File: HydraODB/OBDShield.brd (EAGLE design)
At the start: 59.9 x 37 mm, 10 parts, among them J1 HYDRABUS_SHIELD_CON_HEADER_2X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, J2 HYDRABUS_SHIELD_CON_HEADER_2X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, J3 HYDRABUS_SHIELD_CON_HEADER_2X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, U1 SN65HVD233DG4, U2 SN65HVD233DG4

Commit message: Mistake :-D
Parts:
- added JP1, JP2: (no value), jumper:JP1
- added LPWR, LRXCAN1, LRXCAN2, LTXCAN1, LTXCAN2: (no value), led:CHIPLED_0603
- added R3, R4, R5, R6, R7, R8, R9: (no value), resistor:R0603
- IC1: value (none) -> LM317MABDT; device v-reg:78XXS -> v-reg:DPACK
- moved U1 3.98 mm to (28.8, 14.6), flipped to the top, turned to 90 degrees
- moved SV1 2.41 mm to (4.70, 16.5)
- moved R1 2.32 mm to (18.8, 5.46)
- moved IC1 2.16 mm to (6.48, 30.7), turned to 90 degrees
- moved R2 1.30 mm to (18.0, 31.6)
- moved U2 1.17 mm to (28.8, 23.6), flipped to the top, turned to 90 degrees
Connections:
- new net N$13: LTXCAN1.A, R5.2
- new net N$14: LPWR.A, R3.1
- new net N$15: R3.2
- new net N$16: JP2.1, R9.2
- new net N$19: JP1.1, R8.2
- new net N$7: LRXCAN1.A, R4.2
- new net PB11: J1.4, R9.1, U2.1
- new net PB6: J1.12
- new net PB9: J1.2, JP2.2, U2.4
- net +12V: now also IC1.3, SV1.7, SV1.8; no longer IC1.IN
- net GND: now also IC1.1, LPWR.C, LTXCAN1.C; no longer IC1.GND
- net PB10: now also J1.6, JP1.2, R5.1; no longer J1.8
- net PB5: no longer U2.4
- net PB7: now also J1.10; no longer J1.12, U2.1
- net PB8: now also J1.8, R4.1, R8.1; no longer J1.6
- net VUSB: now also IC1.4; no longer IC1.OUT
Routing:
- net +3V3: track 181.4 -> 0.00 mm
- net PB10: track 152.9 -> 0.00 mm
- net VUSB: track 97.7 -> 0.00 mm
- net PB7: track 38.2 -> 0.00 mm
- net PB5: track 32.3 -> 0.00 mm
- net N$11: track 31.2 -> 0.00 mm
- net N$12: track 28.9 -> 0.00 mm
- net PB8: track 26.2 -> 0.00 mm
- net N$9: track 25.0 -> 0.00 mm
- net N$10: track 24.5 -> 0.00 mm
- net N$17: track 15.4 -> 0.00 mm
- net +12V: track 13.9 -> 0.00 mm
- net N$1: track 8.51 -> 0.00 mm
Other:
- board text added: "HydraCAN Shield 1_0"
- board text removed: "1"
- board text removed: "HydraBus 1_0 Shield Template"
- board text removed: "Template v1.0 Rev0 Sept 2014"

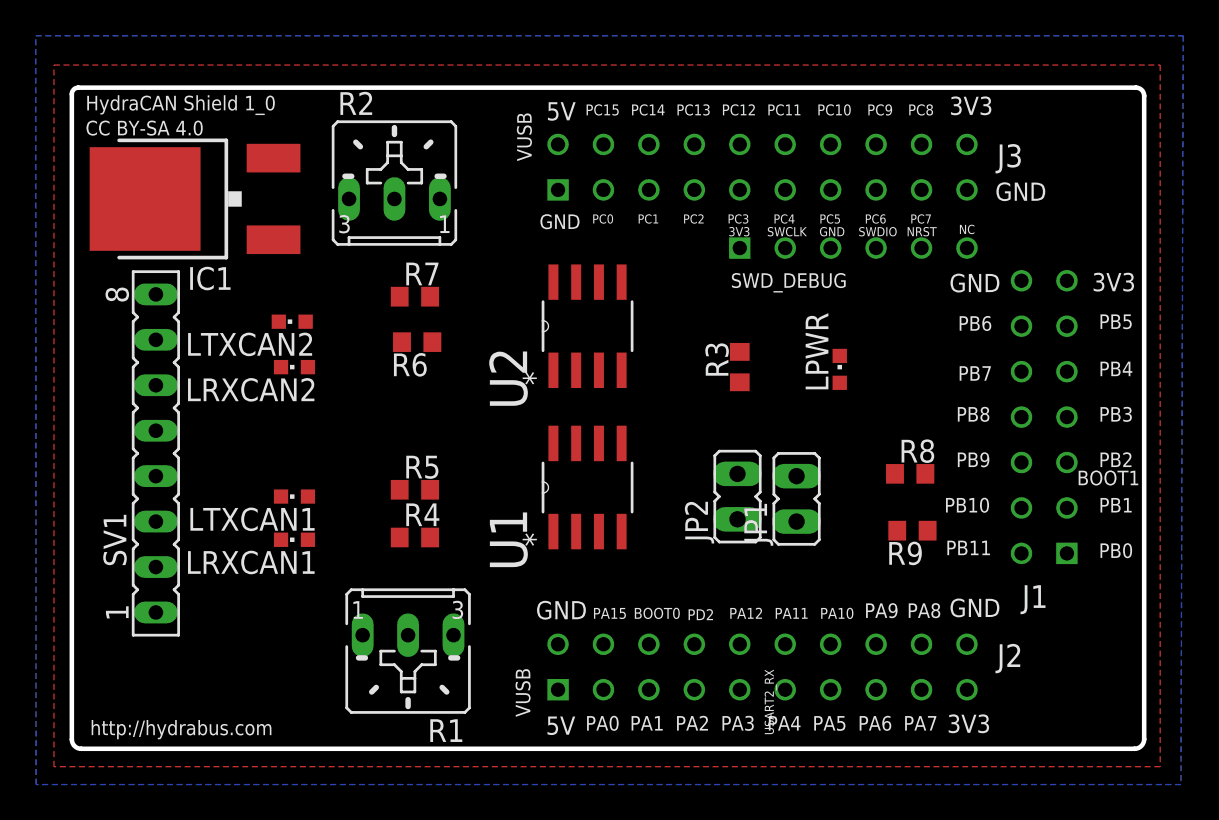
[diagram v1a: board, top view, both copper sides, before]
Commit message: Decoupling caps, user button and different mistakes
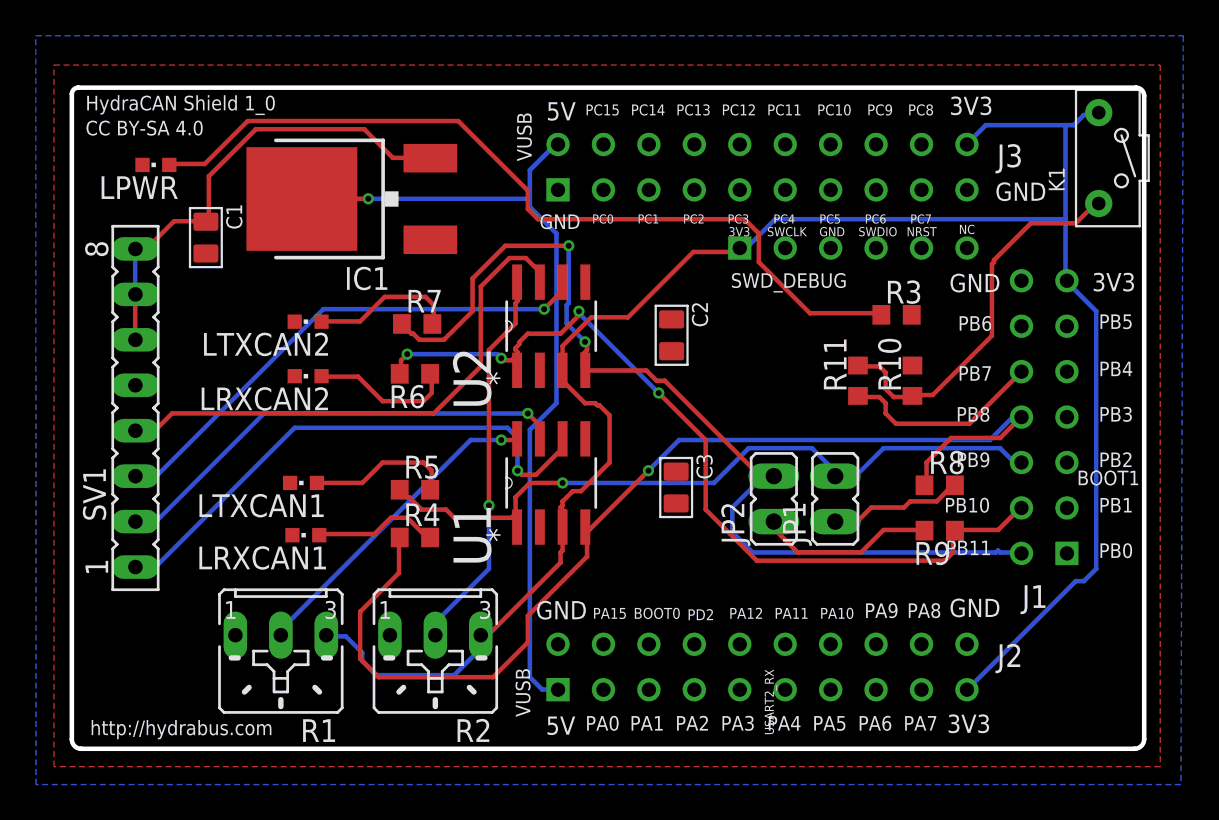
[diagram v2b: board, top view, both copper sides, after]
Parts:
- added C1, C2, C3: 100NF, Seeed-OPL-Capacitor:C0805
- added K1: TS-1101F, Seeed-OPL-Button:SW2-3.4X6.0X3.55MM-90D
- added R10, R11: (no value), resistor:R0603
- moved LPWR 39.9 mm to (4.70, 32.6), turned to 90 degrees
- moved R2 26.3 mm to (20.3, 5.46), turned to 180 degrees
- moved R3 9.24 mm to (46.1, 24.3), turned to 0 degrees
- moved IC1 8.76 mm to (15.2, 30.7)
- moved R1 7.11 mm to (11.7, 5.46)
- moved SV1 2.79 mm to (3.56, 19.1)
- moved JP1 2.16 mm to (42.7, 14.0)
- moved U1 2.05 mm to (26.8, 14.9)
- moved JP2 2.04 mm to (39.2, 14.0)
- moved U2 2.03 mm to (26.8, 23.6)
- moved R6 1.78 mm to (19.2, 21.0)
- moved R8 1.77 mm to (48.5, 14.7)
- moved R7 1.53 mm to (19.3, 23.7)
- moved R9 1.52 mm to (48.5, 12.2)
- moved LTXCAN1 0.92 mm to (13.0, 14.9)
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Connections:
- new net N$21: K1.P$2, R10.1, R11.2
- new net N$22: R10.2
- new net N$4: LRXCAN2.A, R6.1
- new net N$6: LTXCAN2.A, R7.2
- net +12V: now also C1.1
- net +3V3: now also K1.P$1
- net GND: now also C1.2, LRXCAN2.C, LTXCAN2.C
- net PB11: now also R6.2
- net PB7: now also R11.1
- net PB9: now also R7.1
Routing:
- net +3V3: track 0.00 -> 107.4 mm
- net PB8: track 0.00 -> 61.0 mm, vias 0 -> 1
- net PB9: track 0.00 -> 54.8 mm, vias 0 -> 2
- net PB11: track 0.00 -> 48.8 mm, vias 0 -> 4
- net N$14: track 0.00 -> 46.8 mm
- net VUSB: track 0.00 -> 46.4 mm, vias 0 -> 1
- net PB10: track 0.00 -> 40.6 mm, vias 0 -> 1
- net N$9: track 0.00 -> 30.4 mm, vias 0 -> 1
- net N$12: track 0.00 -> 30.1 mm
- net N$11: track 0.00 -> 28.6 mm, vias 0 -> 1
- net +12V: track 0.00 -> 26.5 mm
- net N$10: track 0.00 -> 26.2 mm, vias 0 -> 1
- net N$21: track 0.00 -> 21.7 mm
- net N$17: track 0.00 -> 21.6 mm, vias 0 -> 1
- net N$1: track 0.00 -> 17.9 mm, vias 0 -> 1
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
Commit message: Different corrections and missing wire
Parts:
- moved R10 6.24 mm to (40.8, 20.1)
- moved R11 5.98 mm to (38.0, 20.2), turned to 270 degrees
- moved IC1 1.81 mm to (16.6, 31.9)
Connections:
- removed net N$22: R10.2
- net +3V3: now also C2.2, C3.2
- net GND: now also C2.1, C3.1, LRXCAN1.C, R10.2
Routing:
- net PB8: track 61.0 -> 43.5 mm, vias 1 -> 4
- net N$21: track 21.7 -> 31.4 mm
- net +3V3: track 107.4 -> 116.7 mm
- net PB9: track 54.8 -> 46.7 mm, vias 2 -> 3
- net PB10: track 40.6 -> 47.3 mm, vias 1 -> 3
- net PB7: track 11.3 -> 16.9 mm
- net N$9: track 30.4 -> 35.3 mm, vias 1 -> 0
- net N$17: track 21.6 -> 25.8 mm
- net +12V: track 26.5 -> 28.7 mm
- net N$1: track 17.9 -> 20.1 mm, vias 1 -> 0
- net N$12: track 30.1 -> 28.1 mm
- net VUSB: track 46.4 -> 48.4 mm, vias 1 -> 0
- net PB11: track 48.8 -> 50.3 mm, vias 4 -> 1
- net N$14: track 46.8 -> 48.4 mm, vias 0 -> 2
- net N$7: track 7.07 -> 8.33 mm
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
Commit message: Board modifications, silk screen
Still some work to do on the board
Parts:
- removed SWD_DEBUG: HYDRABUS_SHIELD_CON_HEADER_1X06, hydrabus_shield:HYDRABUS_SHIELD_M1X6
- moved R3 38.4 mm to (8.51, 31.9), turned to 90 degrees
- moved LRXCAN1 33.4 mm to (46.2, 15.9), turned to 0 degrees
- moved LRXCAN2 32.9 mm to (46.1, 22.0), turned to 180 degrees
- moved R9 30.0 mm to (19.7, 20.6), turned to 90 degrees
- moved LTXCAN1 29.4 mm to (42.3, 15.9), turned to 0 degrees
- moved LTXCAN2 29.3 mm to (42.4, 22.0), turned to 180 degrees
- moved K1 29.1 mm to (57.9, 3.94)
- moved R8 28.7 mm to (19.8, 16.1), turned to 90 degrees
- moved JP1 28.0 mm to (14.7, 15.4), turned to 90 degrees
- moved JP2 25.5 mm to (14.9, 21.3), turned to 90 degrees
- moved R4 18.2 mm to (37.0, 15.9)
- moved R5 17.9 mm to (37.0, 12.8)
- moved R6 17.3 mm to (35.8, 25.7), turned to 90 degrees
- moved C1 16.2 mm to (23.6, 30.5)
- moved R10 10.3 mm to (46.2, 11.3)
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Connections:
- removed net NRST: SWD_DEBUG.5
- removed net PB6: J1.12
- removed net PB9: J1.2, JP2.2, R7.1, U2.4
- removed net SWD_SWCLK: SWD_DEBUG.2
- removed net SWD_SWDIO: SWD_DEBUG.4
- removed net VUSB: IC1.4, J2.1, J3.2
- new net N$22: J3.2
- net +12V: no longer SV1.6, SV1.7
- net +3V3: no longer J2.19, J3.20, SWD_DEBUG.1
- net GND: now also SV1.6, SV1.7; no longer J2.20, J3.19, SWD_DEBUG.3
- net N$10: now also R8.1
- net N$11: now also JP2.2
- net N$12: now also R9.1
- net N$15: now also IC1.4
- net N$9: now also JP1.2
- net PB10: no longer JP1.2
- net PB11: now also J1.12; no longer J1.4, R9.1
- net PB5: now also R7.1, U2.4
- net PB8: no longer R8.1
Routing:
- net +3V3: track 116.7 -> 0.00 mm
- net PB11: track 50.3 -> 0.00 mm, vias 1 -> 0
- net VUSB: track 48.4 -> 0.00 mm
- net N$14: track 48.4 -> 0.00 mm, vias 2 -> 0
- net PB10: track 47.3 -> 0.00 mm, vias 3 -> 0
- net PB9: track 46.7 -> 0.00 mm, vias 3 -> 0
- net PB8: track 43.5 -> 0.00 mm, vias 4 -> 0
- net N$9: track 35.3 -> 0.00 mm
- net N$21: track 31.4 -> 0.00 mm
- net N$11: track 29.0 -> 0.00 mm, vias 1 -> 0
- net +12V: track 28.7 -> 0.00 mm
- net N$12: track 28.1 -> 0.00 mm
- net N$10: track 26.4 -> 0.00 mm
- net N$17: track 25.8 -> 0.00 mm, vias 1 -> 0
- net N$1: track 20.1 -> 0.00 mm
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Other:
- board text added: "+12V"
- board text added: "CAN1 H"
- board text added: "CAN1 L"
- board text added: "CAN2 H"
- board text added: "CAN2 L"
- board text removed: "NC"
- board text removed: "NRST"
- board text removed: "SWCLK"
- board text removed: "SWDIO"
- board text removed: "SWD_DEBUG"
